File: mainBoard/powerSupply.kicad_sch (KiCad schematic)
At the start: 24 parts, among them J1 1366005, J2 Conn_01x02, J3 Conn_01x02, SW1 SW_SPST, U1 MCP1727T-3302E/SN

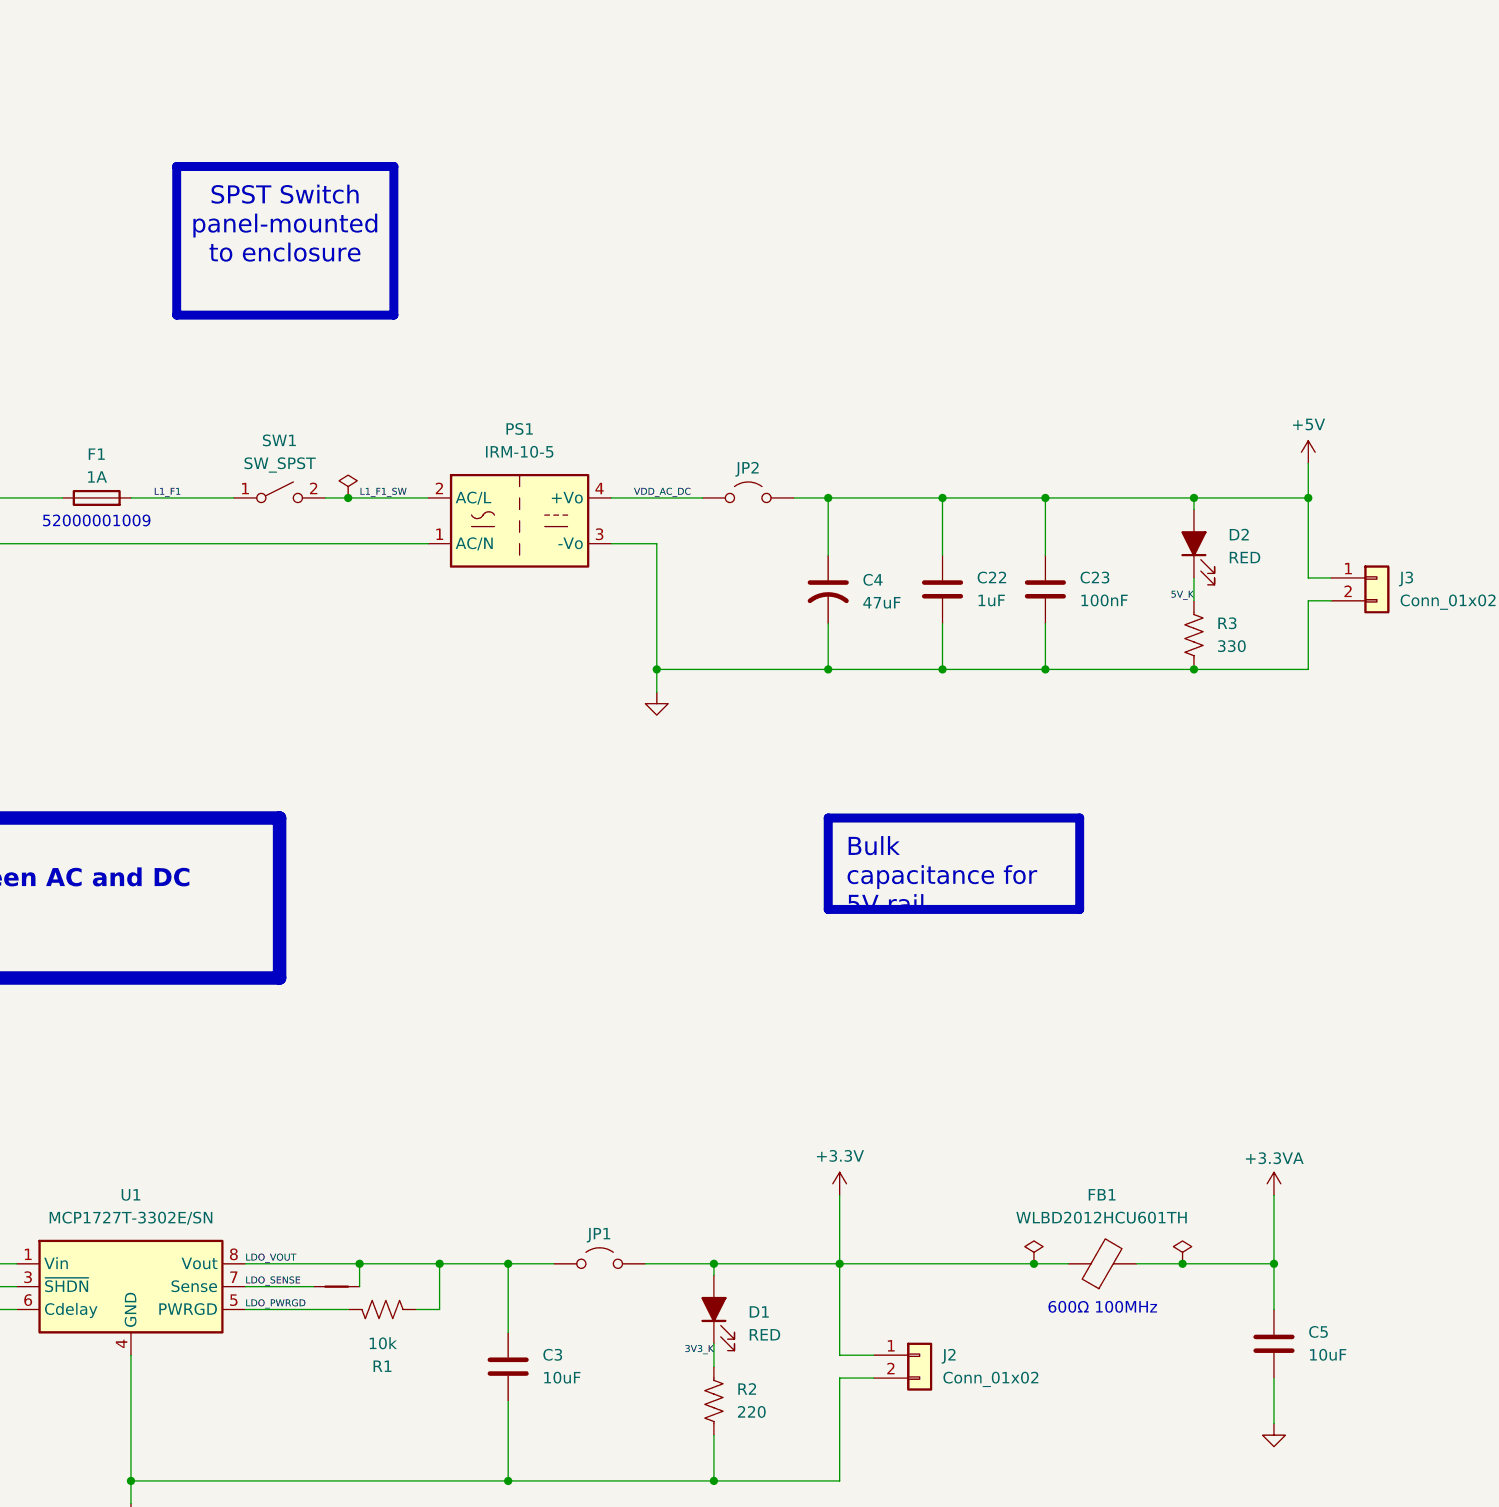
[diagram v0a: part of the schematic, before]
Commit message: Schematic Capture should be complete, ready for PCB
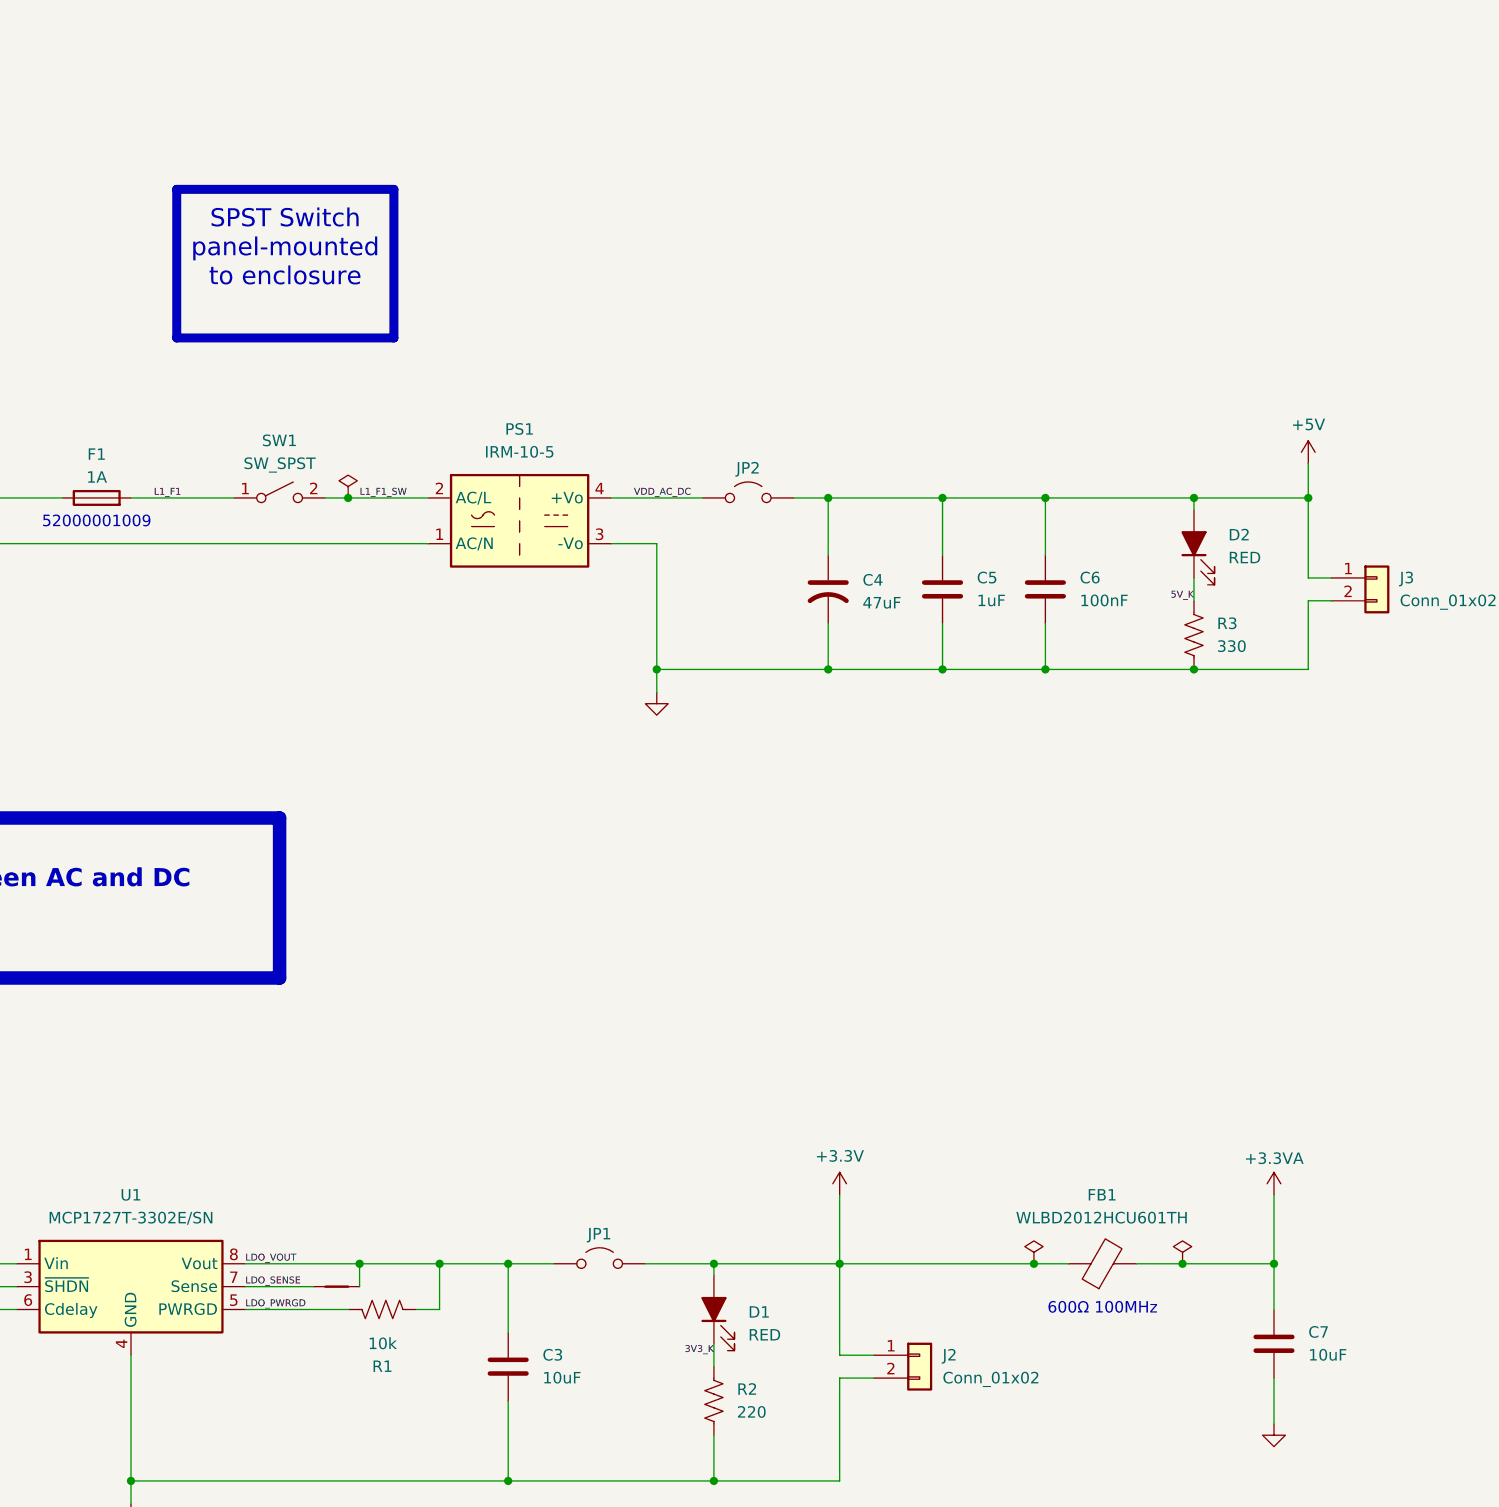
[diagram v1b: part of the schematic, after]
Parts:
- renumbered C22 to C5, C23 to C6, C5 to C7, NT2 to NT1
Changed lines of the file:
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@@
 	(text_box "SPST Switch panel-mounted to enclosure"
 		(exclude_from_sim no)
-		(at 175.26 54.61 0)
+		(at 175.26 57.15 0)
 		(size 24.13 16.51)
 		(margins 2 2 2 2)
@@
 		)
 	)
-	(text_box "Bulk capacitance for 5V rail"
-		(exclude_from_sim no)
-		(at 247.65 127 0)
-		(size 27.94 10.16)
-		(margins 2 2 2 2)
-		(stroke
-			(width 1)
-			(type solid)
-			(color 200 200 200 1)
-		)
-		(fill
-			(type none)
-		)
-		(effects
-			(font
-				(face "Arial")
-				(size 2 2)
-				(color 0 0 0 1)
-			)
-			(justify left top)
-		)
-	)
 	(text_box "HIGH VOLTAGE:\nEnsure appropriate isolation between AC and DC circuits!\n\nAir isolation gap underneath PS1"
 		(exclude_from_sim no)
@@
 		(dnp no)
 		(fields_autoplaced yes)
-		(property "Reference" "#FLG02"
+		(property "Reference" "#FLG04"
 			(at 143.51 174.625 0)
 			(effects
@@
 			(project "mainBoard"
 				(path "/0650c7a8-acba-429c-9f8e-eec0baf0bc1c/fede4c36-00cc-4d3d-b71c-5243ba232202/f08096be-4241-44f0-80c6-822a4bb8e386"
-					(reference "#FLG02")
+					(reference "#FLG04")
 					(unit 1)
 				)
@@
 		(on_board yes)
 		(dnp no)
-		(property "Reference" "#PWR06"
+		(property "Reference" "#PWR02"
 			(at 129.54 88.9 0)
 			(effects
@@
 			(project "mainBoard"
 				(path "/0650c7a8-acba-429c-9f8e-eec0baf0bc1c/fede4c36-00cc-4d3d-b71c-5243ba232202/f08096be-4241-44f0-80c6-822a4bb8e386"
-					(reference "#PWR06")
+					(reference "#PWR02")
 					(unit 1)
 				)
@@
 		(dnp no)
 		(fields_autoplaced yes)
-		(property "Reference" "#PWR05"
+		(property "Reference" "#PWR01"
 			(at 120.65 111.76 0)
 			(effects
@@
 			(project "mainBoard"
 				(path "/0650c7a8-acba-429c-9f8e-eec0baf0bc1c/fede4c36-00cc-4d3d-b71c-5243ba232202/f08096be-4241-44f0-80c6-822a4bb8e386"
-					(reference "#PWR05")
+					(reference "#PWR01")
 					(unit 1)
 				)
@@
 		(dnp no)
 		(fields_autoplaced yes)
-		(property "Reference" "C5"
+		(property "Reference" "C7"
 			(at 300.99 184.1499 0)
 			(effects
@@
 			(project "mainBoard"
 				(path "/0650c7a8-acba-429c-9f8e-eec0baf0bc1c/fede4c36-00cc-4d3d-b71c-5243ba232202/f08096be-4241-44f0-80c6-822a4bb8e386"
-					(reference "C5")
+					(reference "C7")
 					(unit 1)
 				)
@@
 		(dnp no)
 		(fields_autoplaced yes)
-		(property "Reference" "#FLG04"
+		(property "Reference" "#FLG02"
 			(at 120.65 92.075 0)
 			(effects
@@
 			(project "mainBoard"
 				(path "/0650c7a8-acba-429c-9f8e-eec0baf0bc1c/fede4c36-00cc-4d3d-b71c-5243ba232202/f08096be-4241-44f0-80c6-822a4bb8e386"
-					(reference "#FLG04")
+					(reference "#FLG02")
 					(unit 1)
 				)
@@
 		(dnp no)
 		(fields_autoplaced yes)
-		(property "Reference" "#FLG03"
+		(property "Reference" "#FLG01"
 			(at 120.65 85.725 0)
 			(effects
@@
 			(project "mainBoard"
 				(path "/0650c7a8-acba-429c-9f8e-eec0baf0bc1c/fede4c36-00cc-4d3d-b71c-5243ba232202/f08096be-4241-44f0-80c6-822a4bb8e386"
-					(reference "#FLG03")
+					(reference "#FLG01")
 					(unit 1)
 				)
@@
 		(on_board yes)
 		(dnp no)
-		(property "Reference" "#PWR07"
+		(property "Reference" "#PWR03"
 			(at 129.54 99.06 0)
 			(effects
@@
 			(project "mainBoard"
 				(path "/0650c7a8-acba-429c-9f8e-eec0baf0bc1c/fede4c36-00cc-4d3d-b71c-5243ba232202/f08096be-4241-44f0-80c6-822a4bb8e386"
-					(reference "#PWR07")
+					(reference "#PWR03")
 					(unit 1)
 				)
@@
 		(dnp no)
 		(fields_autoplaced yes)
-		(property "Reference" "C22"
+		(property "Reference" "C5"
 			(at 264.16 100.3299 0)
 			(effects
@@
 			(project "mainBoard"
 				(path "/0650c7a8-acba-429c-9f8e-eec0baf0bc1c/fede4c36-00cc-4d3d-b71c-5243ba232202/f08096be-4241-44f0-80c6-822a4bb8e386"
-					(reference "C22")
+					(reference "C5")
 					(unit 1)
 				)
@@
 		(on_board yes)
 		(dnp no)
-		(property "Reference" "#PWR03"
+		(property "Reference" "#PWR04"
 			(at 129.54 172.72 0)
 			(effects
@@
 			(project "mainBoard"
 				(path "/0650c7a8-acba-429c-9f8e-eec0baf0bc1c/fede4c36-00cc-4d3d-b71c-5243ba232202/f08096be-4241-44f0-80c6-822a4bb8e386"
-					(reference "#PWR03")
+					(reference "#PWR04")
 					(unit 1)
 				)
@@
 		(dnp no)
 		(fields_autoplaced yes)
-		(property "Reference" "#FLG01"
+		(property "Reference" "#FLG05"
 			(at 194.31 89.535 0)
 			(effects
@@
 			(project "mainBoard"
 				(path "/0650c7a8-acba-429c-9f8e-eec0baf0bc1c/fede4c36-00cc-4d3d-b71c-5243ba232202/f08096be-4241-44f0-80c6-822a4bb8e386"
-					(reference "#FLG01")
+					(reference "#FLG05")
 					(unit 1)
 				)
@@
 		(dnp no)
 		(fields_autoplaced yes)
-		(property "Reference" "#PWR013"
+		(property "Reference" "#PWR010"
 			(at 297.18 200.66 0)
 			(effects
@@
 			(project "mainBoard"
 				(path "/0650c7a8-acba-429c-9f8e-eec0baf0bc1c/fede4c36-00cc-4d3d-b71c-5243ba232202/f08096be-4241-44f0-80c6-822a4bb8e386"
-					(reference "#PWR013")
+					(reference "#PWR010")
 					(unit 1)
 				)
@@
 		(on_board yes)
 		(dnp no)
-		(property "Reference" "#PWR010"
+		(property "Reference" "#PWR08"
 			(at 248.92 172.72 0)
 			(effects
@@
 			(project "mainBoard"
 				(path "/0650c7a8-acba-429c-9f8e-eec0baf0bc1c/fede4c36-00cc-4d3d-b71c-5243ba232202/f08096be-4241-44f0-80c6-822a4bb8e386"
-					(reference "#PWR010")
+					(reference "#PWR08")
 					(unit 1)
 				)
@@
 		(dnp no)
 		(fields_autoplaced yes)
-		(property "Reference" "NT2"
+		(property "Reference" "NT1"
 			(at 193.04 173.99 0)
 			(effects
@@
 			(project "mainBoard"
 				(path "/0650c7a8-acba-429c-9f8e-eec0baf0bc1c/fede4c36-00cc-4d3d-b71c-5243ba232202/f08096be-4241-44f0-80c6-822a4bb8e386"
-					(reference "NT2")
+					(reference "NT1")
 					(unit 1)
 				)
@@
 		(dnp no)
 		(fields_autoplaced yes)
-		(property "Reference" "#PWR08"
+		(property "Reference" "#PWR06"
 			(at 170.18 209.55 0)
 			(effects
@@
 			(project "mainBoard"
 				(path "/0650c7a8-acba-429c-9f8e-eec0baf0bc1c/fede4c36-00cc-4d3d-b71c-5243ba232202/f08096be-4241-44f0-80c6-822a4bb8e386"
-					(reference "#PWR08")
+					(reference "#PWR06")
 					(unit 1)
 				)
@@
 		(dnp no)
 		(fields_autoplaced yes)
-		(property "Reference" "C23"
+		(property "Reference" "C6"
 			(at 275.59 100.3299 0)
 			(effects
@@
 			(project "mainBoard"
 				(path "/0650c7a8-acba-429c-9f8e-eec0baf0bc1c/fede4c36-00cc-4d3d-b71c-5243ba232202/f08096be-4241-44f0-80c6-822a4bb8e386"
-					(reference "C23")
+					(reference "C6")
 					(unit 1)
 				)
@@
 		(dnp no)
 		(fields_autoplaced yes)
-		(property "Reference" "#PWR04"
+		(property "Reference" "#PWR05"
 			(at 129.54 209.55 0)
 			(effects
@@
 			(project "mainBoard"
 				(path "/0650c7a8-acba-429c-9f8e-eec0baf0bc1c/fede4c36-00cc-4d3d-b71c-5243ba232202/f08096be-4241-44f0-80c6-822a4bb8e386"
-					(reference "#PWR04")
+					(reference "#PWR05")
 					(unit 1)
 				)
@@
 		(dnp no)
 		(fields_autoplaced yes)
-		(property "Reference" "#FLG05"
+		(property "Reference" "#FLG03"
 			(at 121.92 98.425 0)
 			(effects
@@
 			(project "mainBoard"
 				(path "/0650c7a8-acba-429c-9f8e-eec0baf0bc1c/fede4c36-00cc-4d3d-b71c-5243ba232202/f08096be-4241-44f0-80c6-822a4bb8e386"
-					(reference "#FLG05")
+					(reference "#FLG03")
 					(unit 1)
 				)
@@
 		(on_board yes)
 		(dnp no)
-		(property "Reference" "#PWR012"
+		(property "Reference" "#PWR09"
 			(at 297.18 172.72 0)
 			(effects
@@
 			(project "mainBoard"
 				(path "/0650c7a8-acba-429c-9f8e-eec0baf0bc1c/fede4c36-00cc-4d3d-b71c-5243ba232202/f08096be-4241-44f0-80c6-822a4bb8e386"
-					(reference "#PWR012")
+					(reference "#PWR09")
 					(unit 1)
 				)
@@
 		(dnp no)
 		(fields_autoplaced yes)
-		(property "Reference" "#PWR09"
+		(property "Reference" "#PWR07"
 			(at 228.6 119.38 0)
 			(effects
@@
 			(project "mainBoard"
 				(path "/0650c7a8-acba-429c-9f8e-eec0baf0bc1c/fede4c36-00cc-4d3d-b71c-5243ba232202/f08096be-4241-44f0-80c6-822a4bb8e386"
-					(reference "#PWR09")
+					(reference "#PWR07")
 					(unit 1)
 				)
